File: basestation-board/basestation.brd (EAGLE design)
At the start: 72.1 x 44.4 mm, 22 parts, among them IC1 STM32F0, SW1 ROTARTY_ENCODER, U2 MCP73831, X1 BU-SMA-V, X2 RN4020

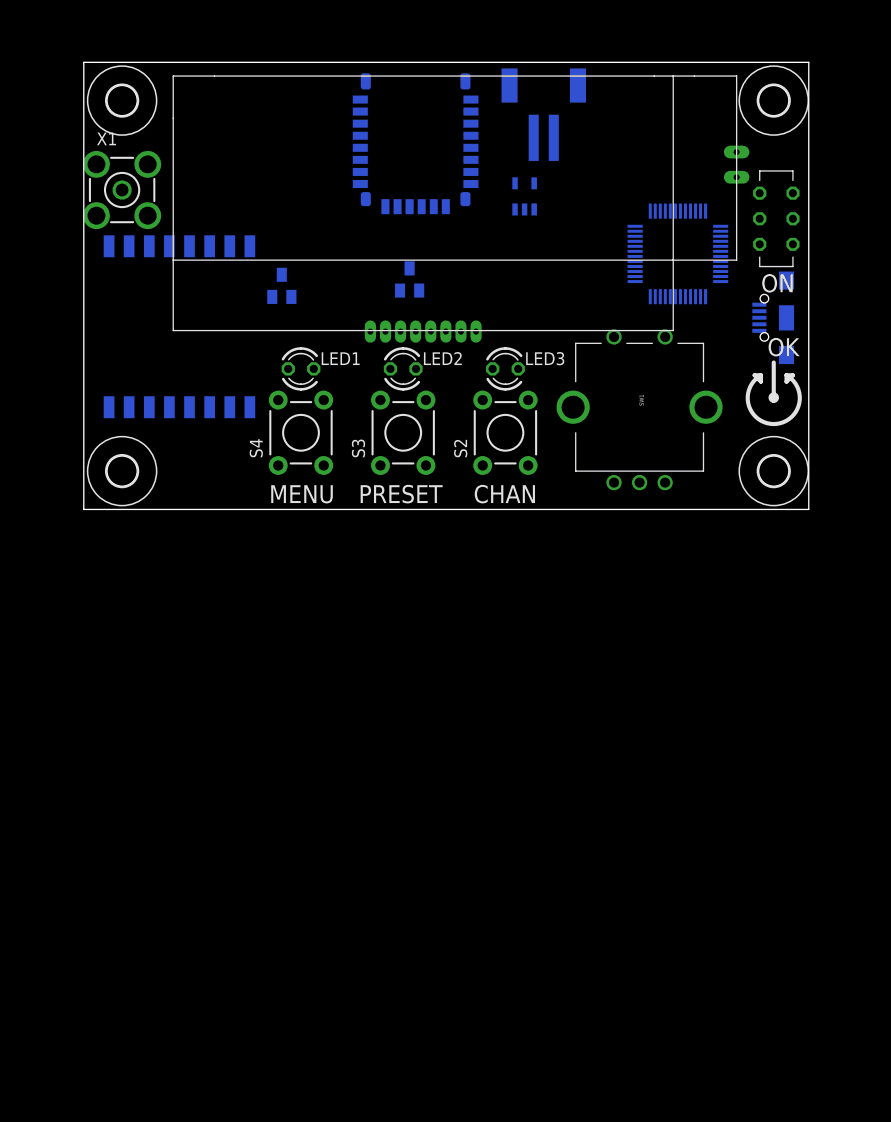
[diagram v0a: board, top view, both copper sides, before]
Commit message: added boot0 to tracker, some wiring on basestation
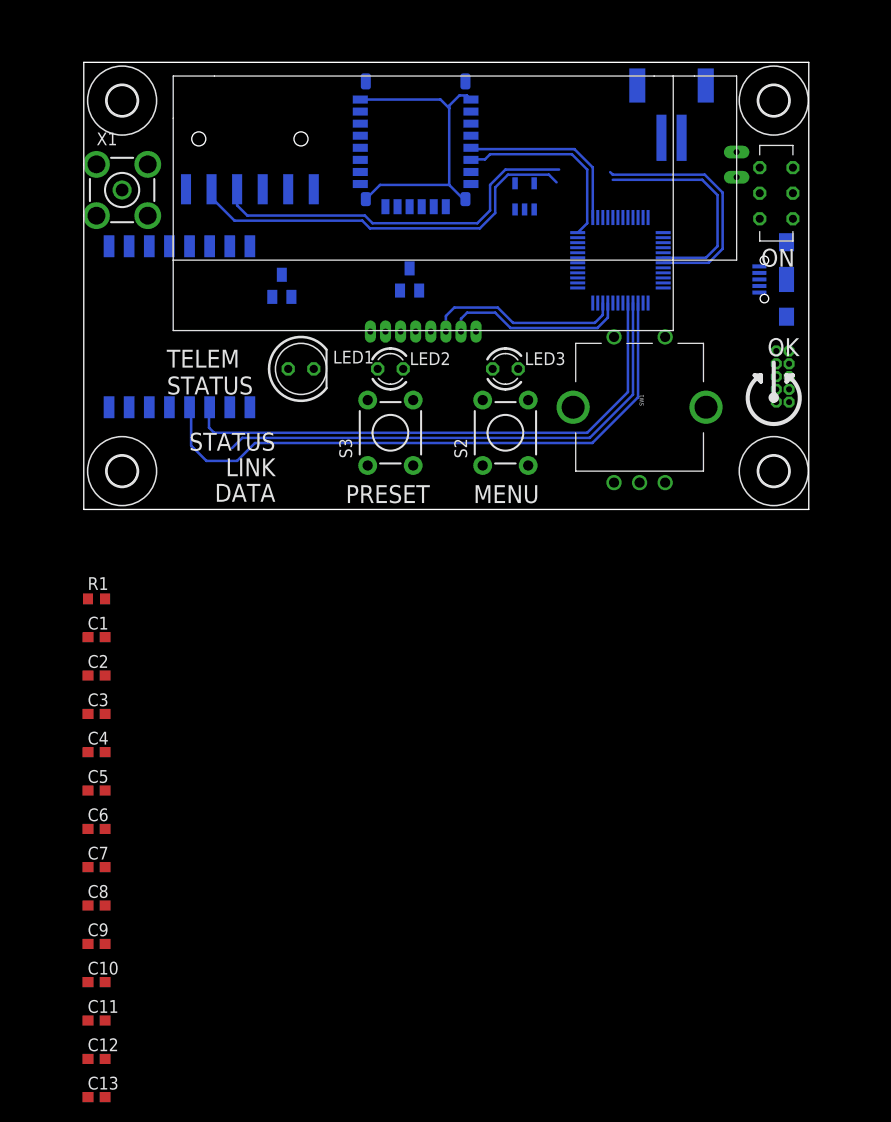
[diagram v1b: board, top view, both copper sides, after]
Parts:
- removed S4: SWITCH-MOMENTARY-2PTH, Mine:TACTILE-PTH
- added C1, C10, C11, C12, C13, C2, C3, C4, C5, C6, C7, C8, C9: (no value), resistor:C0603
- added J2: SWD_PTH_SHROUD, dtb:SWD_PTH_SHROUD
- added JP2: (no value), SparkFun-Connectors:1X06-SMD
- added R1: (no value), resistor:R0603
- LED1: device led:LED3MM -> led:LED5MM
- moved J1 12.7 mm to (58.4, 40.6)
- moved IC1 5.75 mm to (53.3, 24.8), turned to 90 degrees
- moved JP1 3.81 mm to (69.8, 22.9)
- moved U$5 2.54 mm to (70.5, 31.4)
- moved LED2 1.27 mm to (30.5, 14.0)
- moved S3 1.27 mm to (30.5, 7.62)
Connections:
- removed net VBAT: U2.3
- removed net VDD: IC1.24, U$2.5
- removed net VDD(VBAT): IC1.1
- removed net VDD1: IC1.48
- removed net VDDA: IC1.9
- removed net VIN: U2.4
- removed net VSS: IC1.23, U$2.4, U2.2
- removed net VSS1: IC1.47
- removed net VSSA: IC1.8
- new net +3V3: C12.2, C13.2, C2.2, C3.2, C4.2, C5.2, C6.2, IC1.1, IC1.24, IC1.48, IC1.9, J2.1, JP2.4, U$2.5, U$4.2, X2.23
- new net 3.3V: C10.2, U$1.13, U$3.2
- new net DM: IC1.32, JP1.D-1
- new net DP: IC1.33, JP1.D+1
- new net GND: C10.1, C11.1, C12.1, C13.1, C2.1, C3.1, C4.1, C5.1, C6.1, C7.1, C8.1, C9.1, IC1.23, IC1.47, IC1.8, J1.1, J2.3, J2.5, J2.9, JP1.GND1, JP2.6, R1.1, U$1.1, U$1.10, U$1.8, U$2.4, U$3.1, U$4.1, U2.2, X2.1, X2.16, X2.24, X2.9
- new net MISO: IC1.40, U$1.2
- new net MOSI: IC1.41, U$1.3
- new net N$2: C8.2, J1.2, U$5.2X, U2.3
- new net N$3: C7.2, U$4.3, U$5.2A
- new net N$4: IC1.44, R1.2
- new net N$5: C11.2, U$3.3
- new net N$7: C9.2, U2.4
- new net N$8: C1.1, U$2.8
- new net N$9: C1.2, U$2.7
- new net NSS: U$1.5
- new net RST: IC1.7, J2.10
- new net SCL: IC1.45, U$2.2
- new net SCLK: IC1.39, U$1.4
- new net SDA: IC1.46, U$2.3
- new net SWCLK: IC1.37, J2.4
- new net SWDAT: IC1.34, J2.2
- new net S_RST: U$2.1
- new net USART1_RX: IC1.31, JP2.3
- new net USART1_TX: IC1.30, JP2.2
- new net USART2_RX: IC1.13, X2.5
- new net USART2_TX: IC1.12, X2.6
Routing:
- net USART1_TX: track 0.00 -> 62.4 mm
- net USART1_RX: track 0.00 -> 62.1 mm
- net SCLK: track 0.00 -> 60.9 mm
- net MOSI: track 0.00 -> 54.4 mm
- net MISO: track 0.00 -> 51.2 mm
- net GND: track 0.00 -> 30.9 mm
- net SDA: track 0.00 -> 19.6 mm
- net USART2_TX: track 0.00 -> 19.1 mm
- net SCL: track 0.00 -> 18.6 mm
- net USART2_RX: track 0.00 -> 17.9 mm
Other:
- board text added: "DATA"
- board text added: "LINK"
- board text added: "STATUS"
- board text added: "TELEM STATUS"
- board text removed: "CHAN"

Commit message: initial route
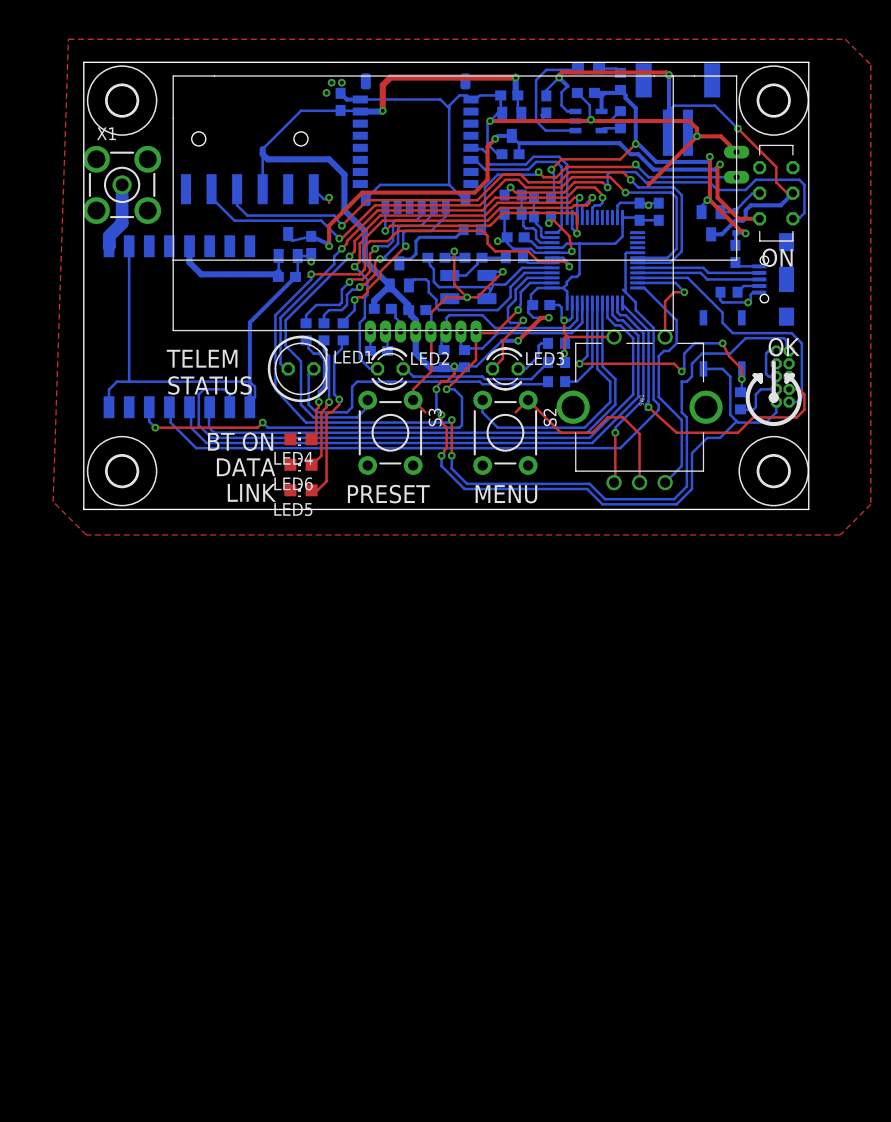
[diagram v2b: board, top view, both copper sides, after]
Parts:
- added C14, C15, C16: (no value), resistor:C0603
- added D1: BAT760, dtb:SOD323-R
- added L1: (no value), SparkFun-Passives:0603
- added LED4, LED5, LED6, LED7: (no value), led:CHIP-LED0805
- added Q1, Q2: BSS84, transistor-small-signal:SOT23
- added R10, R11, R12, R13, R14, R15, R16, R17, R18, R2, R3, R4, R5, R6, R7, R8, R9: (no value), resistor:R0603
- added S1: SWITCH-MOMENTARY-2SMD, Mine:TACTILE_SWITCH_SMD
- added U$6: CRYSTAL-GROUNDED, SparkFun-FreqCtrl:CRYSTAL-SMD-5X3
- C13, C8, C9: value (none) -> 4u7
- moved C13 107.7 mm to (42.3, 41.1), flipped to the bottom, turned to 180 degrees
- moved C9 97.6 mm to (49.9, 41.4), flipped to the bottom, turned to 180 degrees
- moved C8 91.3 mm to (46.0, 40.3), flipped to the bottom, turned to 90 degrees
- moved C7 81.9 mm to (42.4, 35.3), flipped to the bottom, turned to 180 degrees
- moved C12 81.0 mm to (33.1, 19.8), flipped to the bottom
- moved C5 80.2 mm to (57.1, 29.6), flipped to the bottom, turned to 270 degrees
- moved C11 80.0 mm to (22.6, 26.3), flipped to the bottom, turned to 90 degrees
- moved C6 76.2 mm to (25.5, 40.5), flipped to the bottom, turned to 270 degrees
- moved C3 73.5 mm to (55.2, 29.6), flipped to the bottom, turned to 270 degrees
- moved C10 72.6 mm to (20.2, 23.1), flipped to the bottom
- moved R1 67.0 mm to (65.3, 10.8), flipped to the bottom, turned to 90 degrees
- moved C4 62.7 mm to (45.5, 20.3), flipped to the bottom
- moved C2 60.3 mm to (42.9, 27.1), flipped to the bottom, turned to 180 degrees
- moved C1 40.0 mm to (29.3, 15.7), flipped to the bottom, turned to 180 degrees
- moved U$4 27.9 mm to (42.5, 38.2), turned to 180 degrees
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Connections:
- removed net S_RST: U$2.1
- new net AIN1: IC1.11, R14.1, R15.2
- new net BACK_EN: IC1.4, Q1.1
- new net LED1: IC1.16, LED2.A
- new net LED2: IC1.3, LED3.A
- new net LED3: IC1.18, LED1.A
- new net LED4: IC1.43, R4.1
- new net N$10: LED3.K, R3.2
- new net N$11: LED1.K, R4.2
- new net N$12: C14.1, U$2.6
- new net N$13: R11.2, X2.11
- new net N$14: R9.2, X2.12
- new net N$15: LED5.A, R10.1
- new net N$16: LED6.A, R11.1
- new net N$17: LED4.A, R9.1
- new net N$18: X2.7
- new net N$19: X2.8
- new net N$23: R5.1, U$2.A
- new net N$27: IC1.10, R12.1, R13.2
- new net N$28: JP1.ID1, R16.1
- new net N$29: LED7.C, U2.1
- new net N$30: IC1.6, R17.2
- new net N$31: C16.2, IC1.5, U$6.1
- new net N$32: C15.2, R17.1, U$6.3
- new net N$33: C8.2, J1.2, Q2.3, U$5.1X, U2.3
- new net N$34: LED7.A, R8.2
- new net N$35: JP1.VBUS1, L1.2
- new net N$6: LED2.K, R2.2
- new net P_RST: IC1.2, U$1.6, U$2.1
- new net ROT_A: IC1.36, SW1.B
- new net ROT_B: IC1.38, SW1.A
- new net ROT_M: IC1.35, SW1.SW+
- new net SW1: IC1.42, S2.3
- new net SW2: IC1.15, S3.3
- new net VBAT_S: R12.2, U$5.1A
- new net VBUS: C9.2, D1.A, L1.1, Q2.1, R14.2, R8.1, U2.4
- new net VIN_S: C11.2, C7.2, U$3.3, U$4.3, U$5.2A
- new net WAKE: IC1.14, X2.15
- net +3V3: now also C14.2, Q1.2, R6.1, R7.1, S1.3
- net GND: now also C15.1, C16.1, LED4.C, LED5.C, LED6.C, R13.1, R15.1, R16.2, R18.2, R2.1, R3.1, S2.1, S3.1, SW1.C, SW1.SW-, U$2.K, U$6.2, U$6.4
- net N$2: now also D1.C, Q2.2; no longer C8.2, J1.2, U2.3
- net N$3: now also Q1.3, R5.2; no longer C7.2, U$4.3, U$5.2A
- net N$4: now also S1.1
- net N$5: now also R10.2, X2.10; no longer C11.2, U$3.3
- net N$7: now also R18.1, U2.5; no longer C9.2, U2.4
- net NSS: now also IC1.29
- net SCL: now also R7.2
- net SDA: now also R6.2
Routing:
- net GND: track 30.9 -> 252.1 mm, vias 0 -> 18
- net +3V3: track 0.00 -> 181.4 mm, vias 0 -> 8
- net RST: track 0.00 -> 120.4 mm, vias 0 -> 4
- net NSS: track 0.00 -> 71.2 mm
- net VIN_S: track 0.00 -> 62.5 mm, vias 0 -> 3
- net P_RST: track 0.00 -> 55.4 mm, vias 0 -> 4
- net SW2: track 0.00 -> 54.2 mm, vias 0 -> 2
- net N$33: track 0.00 -> 53.9 mm, vias 0 -> 3
- net LED3: track 0.00 -> 46.8 mm, vias 0 -> 2
- net VBUS: track 0.00 -> 44.8 mm, vias 0 -> 5
- net LED1: track 0.00 -> 42.4 mm, vias 0 -> 2
- net VBAT_S: track 0.00 -> 38.0 mm, vias 0 -> 2
- net SWCLK: track 0.00 -> 32.9 mm, vias 0 -> 1
- net N$23: track 0.00 -> 32.3 mm, vias 0 -> 2
- net N$11: track 0.00 -> 30.5 mm
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- added copper zone on layer 1, net GND
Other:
- board text added: "BT ON"
- board text removed: "STATUS"

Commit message: adding interrupt line to raido
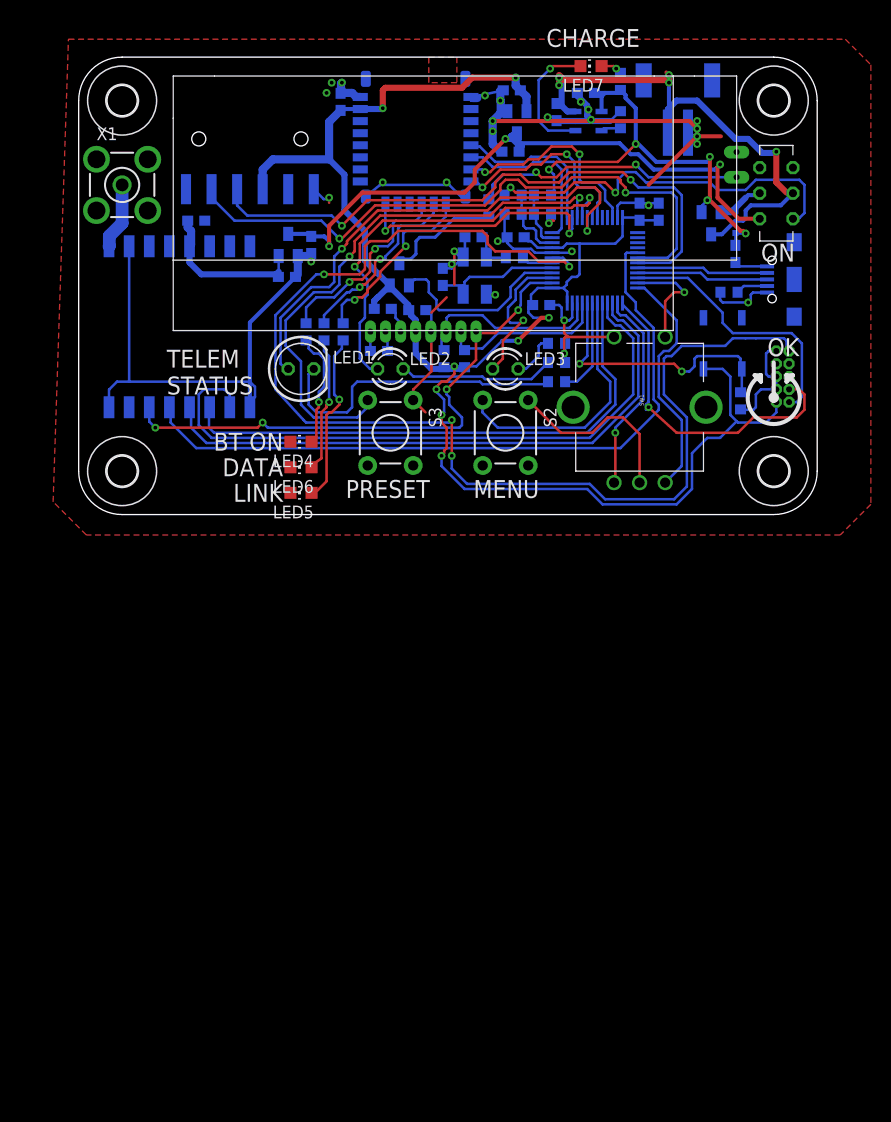
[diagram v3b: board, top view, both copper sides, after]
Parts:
- removed U$2: NHD-C0216CIZ-FSW, dtb:NHD-C0216CIZ-FSW
- removed U$4: MCP1700TT, dtb:SOT23
- removed U$6: CRYSTAL-GROUNDED, SparkFun-FreqCtrl:CRYSTAL-SMD-5X3
- added C17: 100n, resistor:C0603
- added IC2: MCP1700TT, dtb:SOT23
- added IC3: MCP73831, SparkFun-PowerIC:SOT23-5
- added U3: RN4020, Mine:RN4020
- C10, C11: value (none) -> 4u7
- U2: value MCP73831 -> NHD-C0216CIZ-FSW; device SparkFun-PowerIC:SOT23-5 -> dtb:NHD-C0216CIZ-FSW
- X2: value RN4020 -> CRYSTAL-GROUNDED; device Mine:RN4020 -> SparkFun-FreqCtrl:CRYSTAL-SMD-5X3
- moved U2 46.2 mm to (8.89, 17.8), flipped to the top, turned to 0 degrees
- moved X2 6.61 mm to (38.9, 23.2), turned to 90 degrees
- moved R5 2.72 mm to (40.3, 30.0), turned to 270 degrees
- moved C15 2.03 mm to (38.7, 27.1)
- moved C16 2.01 mm to (35.7, 23.1), turned to 270 degrees
- moved C8 1.27 mm to (47.0, 39.5)
- moved JP1 0.76 mm to (70.6, 22.9)
- moved C13 0.57 mm to (42.5, 41.7)
- moved LED7 0.36 mm to (50.4, 44.1), flipped to the top, turned to 90 degrees
- moved C7 0.25 mm to (42.4, 35.6)
- moved R14 0.25 mm to (45.6, 31.2)
- moved R15 0.25 mm to (45.6, 29.3)
- moved LED4 0.25 mm to (21.6, 6.73)
- moved LED6 0.25 mm to (21.6, 4.19)
- moved LED5 0.25 mm to (21.6, 1.65)
- renumbered U$1 to U1, U$3 to IC4
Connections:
- removed net N$18: X2.7
- removed net N$19: X2.8
- new net CMD: IC1.19, U3.8
- new net WAKE_SW: IC1.22, U3.7
- net +3V3: now also IC2.2, U2.5, U3.23; no longer U$2.5, U$4.2, X2.23
- net 3.3V: now also C17.2
- net GND: now also C17.1, IC2.1, IC3.2, U2.4, U2.K, U3.1, U3.16, U3.24, U3.9, X1.2, X1.3, X1.4, X1.5, X2.2, X2.4; no longer U$2.4, U$2.K, U$4.1, U$6.2, U$6.4, U2.2, X2.1, X2.16, X2.24, X2.9
- net LED3: now also IC1.17; no longer IC1.18
- net N$12: now also U2.6; no longer U$2.6
- net N$13: now also U3.11; no longer X2.11
- net N$14: now also U3.12; no longer X2.12
- net N$23: now also U2.A; no longer U$2.A
- net N$29: now also IC3.1; no longer U2.1
- net N$31: now also X2.1; no longer U$6.1
- net N$32: now also X2.3; no longer U$6.3
- net N$33: now also IC3.3; no longer U2.3
- net N$5: now also U3.10; no longer X2.10
- net N$7: now also IC3.5; no longer U2.5
- net N$8: now also U2.8; no longer U$2.8
- net N$9: now also U2.7; no longer U$2.7
- net P_RST: now also U2.1; no longer U$2.1
- net SCL: now also U2.2; no longer U$2.2
- net SDA: now also U2.3; no longer U$2.3
- net USART2_RX: now also U3.5; no longer X2.5
- net USART2_TX: now also U3.6; no longer X2.6
- net VBUS: now also IC3.4; no longer U2.4
- net VIN_S: now also IC2.3; no longer U$4.3
- net WAKE: now also U3.15; no longer X2.15
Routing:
- net GND: track 252.1 -> 216.3 mm, vias 18 -> 29
- net WAKE_SW: track 0.00 -> 20.8 mm, vias 0 -> 2
- net CMD: track 0.00 -> 19.8 mm, vias 0 -> 2
- net +3V3: track 181.4 -> 176.2 mm
- net N$31: track 16.7 -> 12.8 mm
- net LED3: track 46.8 -> 50.2 mm
- net N$3: track 8.52 -> 11.8 mm
- net N$23: track 32.3 -> 29.5 mm
- net N$33: track 53.9 -> 56.7 mm, vias 3 -> 5
- net 3.3V: track 13.2 -> 15.9 mm
- net N$32: track 6.51 -> 4.10 mm
- net N$4: track 29.9 -> 27.7 mm, vias 4 -> 2
- net RST: track 120.4 -> 122.5 mm
- net SW2: track 54.2 -> 55.2 mm
- net WAKE: track 26.2 -> 25.2 mm
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- added copper zone on layer 1, net N$18
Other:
- board size 72.1 x 44.4 mm -> 73.4 x 45.5 mm
- board text added: "BOOT"
- board text added: "CHARGE"

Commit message: minor changes
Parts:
- added U$1: MMBZ27VCLT1, SparkFun-DiscreteSemi:SOT23-3
- added U$2: NUP2114UCMR6T1G, Mine:TSOP6
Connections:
- new net R_INT: IC1.28, U1.14
- net DM: now also U$2.1
- net DP: now also U$2.6
- net GND: now also U$2.2
- net N$1: now also U$1.3
- net N$35: now also U$2.5
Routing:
- net R_INT: track 0.00 -> 109.5 mm, vias 0 -> 8
- net GND: track 216.3 -> 225.0 mm, vias 29 -> 86
- net RST: track 122.5 -> 121.3 mm
- net ROT_A: track 24.0 -> 23.4 mm
- net ROT_M: track 10.9 -> 10.3 mm
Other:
- board text removed: "CHARGE"

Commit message: some stuff changed lol
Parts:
- removed R16: (no value), resistor:R0603
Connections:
- net GND: no longer R16.2
- net N$28: no longer R16.1
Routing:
- net N$28: track 3.18 -> 2.31 mm

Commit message: poking some routing
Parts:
- moved C5 15.7 mm to (45.5, 19.1), turned to 0 degrees
- moved C7 1.52 mm to (42.4, 37.1)
- moved IC2 1.52 mm to (43.1, 40.0)
- moved C13 1.27 mm to (42.5, 42.9)
- moved C9 1.27 mm to (49.9, 42.7)
- moved C8 1.02 mm to (47.0, 40.5)
- moved C4 0.76 mm to (45.5, 21.1)
- moved IC3 0.76 mm to (50.2, 39.4)
- moved J1 0.51 mm to (59.1, 41.7)
- moved R9 0.25 mm to (21.8, 17.7)
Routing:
- net +3V3: track 176.2 -> 192.7 mm, vias 8 -> 6
- net GND: track 224.9 -> 213.9 mm, vias 86 -> 117
- net VIN_S: track 63.2 -> 65.6 mm
- net N$28: track 2.31 -> 0.00 mm
- net LED2: track 15.3 -> 13.6 mm
- net N$33: track 56.7 -> 55.8 mm
- net N$29: track 12.8 -> 12.1 mm
- added copper zone on layer 16, net GND

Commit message: proded silk
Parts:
- removed U$1: MMBZ27VCLT1, SparkFun-DiscreteSemi:SOT23-3
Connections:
- net N$1: no longer U$1.3
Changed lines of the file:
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@@
 <text x="38.735" y="1.143" size="1.778" layer="21" font="vector" ratio="13">MENU</text>
 <text x="26.035" y="1.143" size="1.778" layer="21" font="vector" ratio="13">PRESET</text>
-<wire x1="69.85" y1="13.335" x2="67.31" y2="13.335" width="0.4064" layer="21" curve="-301.263732"/>
+<wire x1="69.85" y1="13.335" x2="67.31" y2="13.335" width="0.6096" layer="21" curve="-301.263732"/>
 <text x="67.945" y="15.24" size="1.778" layer="21" font="vector" ratio="13">OK</text>
-<wire x1="68.58" y1="10.795" x2="68.58" y2="14.605" width="0.4064" layer="21"/>
-<wire x1="69.85" y1="12.7" x2="69.85" y2="13.335" width="0.4064" layer="21"/>
-<wire x1="69.85" y1="13.335" x2="70.485" y2="13.335" width="0.4064" layer="21"/>
-<wire x1="70.485" y1="13.335" x2="69.85" y2="12.7" width="0.4064" layer="21"/>
-<wire x1="67.31" y1="13.335" x2="66.675" y2="13.335" width="0.4064" layer="21"/>
-<wire x1="66.675" y1="13.335" x2="67.31" y2="12.7" width="0.4064" layer="21"/>
-<wire x1="67.31" y1="12.7" x2="67.31" y2="13.335" width="0.4064" layer="21"/>
-<circle x="68.58" y="11.1125" radius="0.3175" width="0.4064" layer="21"/>
+<wire x1="68.58" y1="10.795" x2="68.58" y2="14.605" width="0.3048" layer="21"/>
+<wire x1="69.85" y1="13.335" x2="70.993" y2="13.335" width="0.6096" layer="21"/>
+<wire x1="70.993" y1="13.335" x2="69.85" y2="12.446" width="0.6096" layer="21"/>
+<wire x1="67.31" y1="13.335" x2="66.167" y2="13.335" width="0.6096" layer="21"/>
+<wire x1="66.167" y1="13.335" x2="67.31" y2="12.446" width="0.6096" layer="21"/>
+<wire x1="67.31" y1="12.446" x2="67.31" y2="13.335" width="0.6096" layer="21"/>
+<circle x="68.58" y="11.1125" radius="0.3175" width="0.6096" layer="21"/>
 <text x="67.31" y="24.638" size="1.778" layer="21" font="vector" ratio="13">ON</text>
 <text x="19.812" y="7.62" size="1.778" layer="21" font="vector" ratio="13" rot="R180">BT ON</text>
@@
 <wire x1="51.308" y1="31.75" x2="48.006" y2="31.75" width="0.1524" layer="22"/>
 <wire x1="48.006" y1="31.75" x2="48.006" y2="32.004" width="0.1524" layer="22"/>
+<dimension x1="3.81" y1="-0.508" x2="3.81" y2="44.958" x3="-14.224" y3="22.225" textsize="1.778" layer="16"/>
+<dimension x1="-0.508" y1="40.64" x2="72.898" y2="40.64" x3="36.195" y3="53.848" textsize="1.778" layer="16"/>
+<wire x1="69.85" y1="13.208" x2="69.85" y2="12.446" width="0.6096" layer="21"/>
 </plain>
 <attributes>
@@
 <attribute name="NAME" x="12.827" y="29.083" size="1.016" layer="26" font="vector" ratio="13" rot="MR180"/>
 </element>
-<element name="U$1" library="SparkFun-DiscreteSemi" package="SOT23-3" value="MMBZ27VCLT1" x="-4.826" y="-1.016"/>
 <element name="U$2" library="Mine" package="TSOP6" value="NUP2114UCMR6T1G" x="74.168" y="24.638" rot="MR180"/>
 </elements>
@@
 <wire x1="2.54" y1="27.178" x2="2.54" y2="26.19" width="1.27" layer="16"/>
 <wire x1="2.54" y1="26.19" x2="2.51" y2="26.16" width="1.27" layer="16"/>
-<contactref element="U$1" pad="3"/>
-<wire x1="-4.826" y1="0.084" x2="2.51" y2="26.16" width="0" layer="19" extent="1-16"/>
 </signal>
 <signal name="+3V3">
